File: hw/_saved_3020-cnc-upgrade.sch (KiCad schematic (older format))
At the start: 11 parts, among them P1 CONN_01X02, P2 CONN_01X03, P3 CONN_01X08, P4 CONN_01X03, U1 6N136, U2 arduino_pro_micro, U3 MCP41010

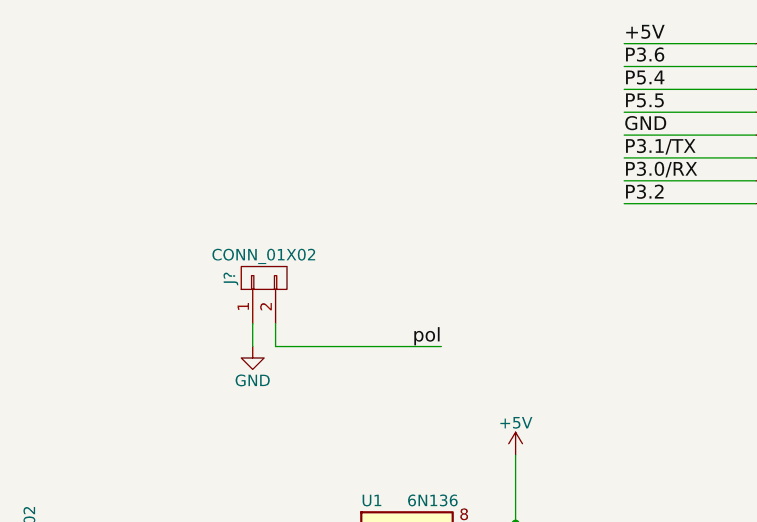
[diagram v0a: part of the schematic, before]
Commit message: added jumper to reverse spindle polarity
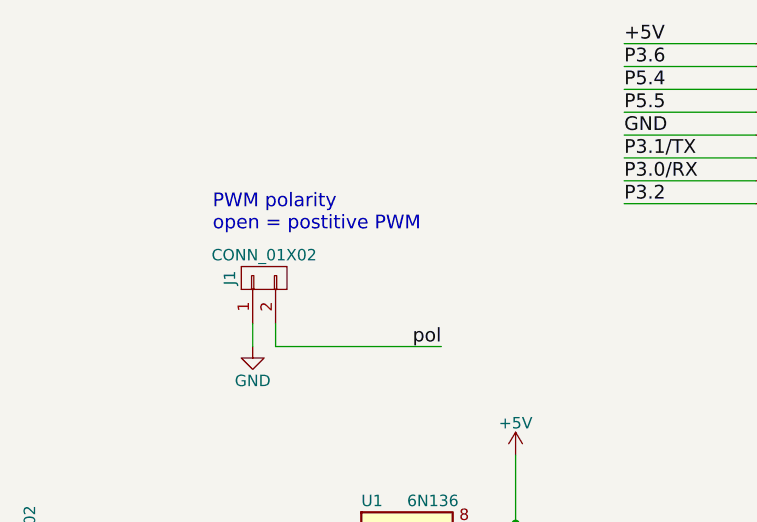
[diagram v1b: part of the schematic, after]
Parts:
- J1: renamed from J?; footprint (none) -> Pin_Headers:Pin_Header_Straight_1x02_Pitch2.54mm
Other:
- note added: "PWM polarity\nopen = postitive PWM\n"
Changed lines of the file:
@@
 ~CS
 $Comp
-L CONN_01X02 J?
+L CONN_01X02 J1
 U 1 1 5ABA669E
 P 2250 2400
-F 0 "J?" H 2250 2550 50  0000 C CNN
+F 0 "J1" H 2250 2550 50  0000 C CNN
 F 1 "CONN_01X02" V 2350 2400 50  0000 C CNN
-F 2 "" H 2250 2400 50  0001 C CNN
+F 2 "Pin_Headers:Pin_Header_Straight_1x02_Pitch2.54mm" H 2250 2400 50  0001 C CNN
 F 3 "" H 2250 2400 50  0001 C CNN
 	1    2250 2400
@@
 $EndComp
 $Comp
-L GND #PWR?
+L GND #PWR05
 U 1 1 5ABA677C
 P 2200 2700
-F 0 "#PWR?" H 2200 2450 50  0001 C CNN
+F 0 "#PWR05" H 2200 2450 50  0001 C CNN
 F 1 "GND" H 2200 2550 50  0000 C CNN
 F 2 "" H 2200 2700 50  0000 C CNN
@@
 Text Label 4275 3875 0    60   ~ 0
 pol
+Text Notes 2025 2200 0    60   ~ 0
+PWM polarity\nopen = postitive PWM\n
 $EndSCHEMATC
